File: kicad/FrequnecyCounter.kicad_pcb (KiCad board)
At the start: 4 copper layers, 130 x 90 mm, 138 parts, among them J1 USB_B, J2 CONN_COAXIAL, J3 CONN_COAXIAL, J4 CONN_COAXIAL, SW1 SW_Push, T1 WBC16-1T, U1 TPS650250, U10 MC12093, U11 tx176, U12 TLV3501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

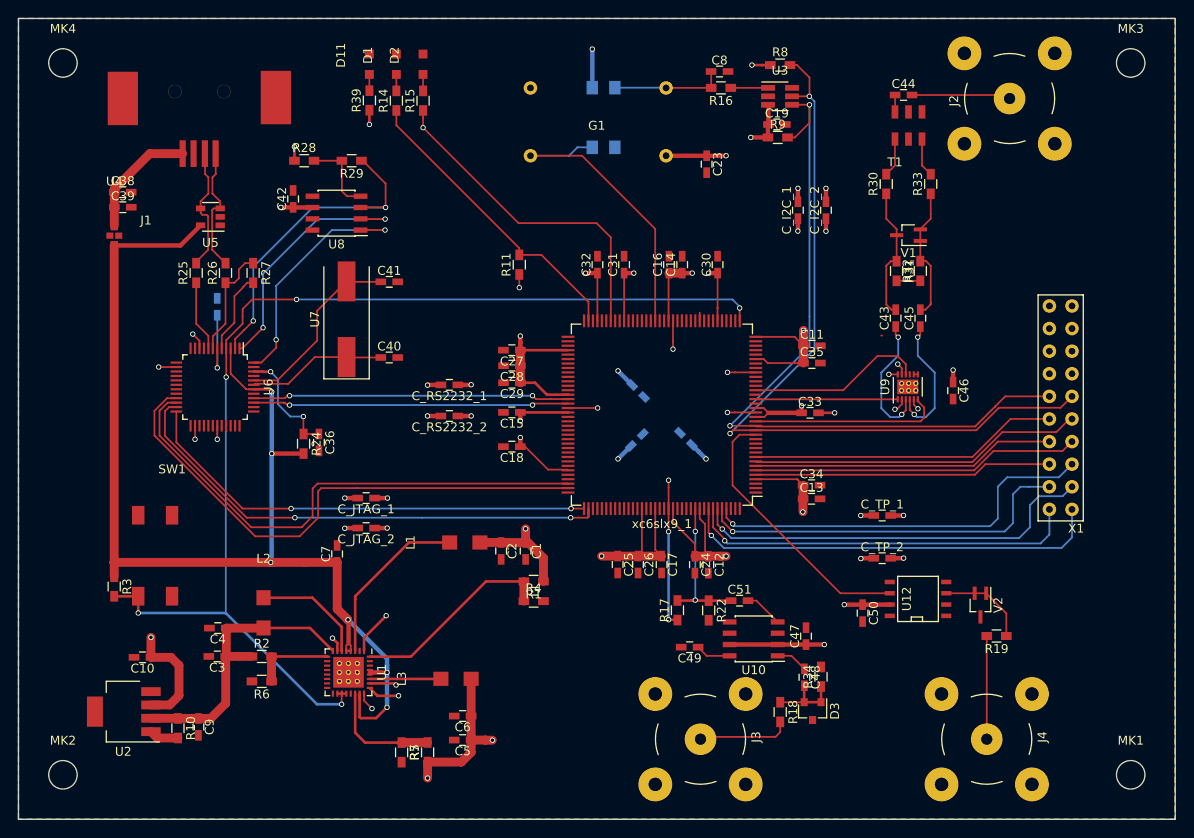
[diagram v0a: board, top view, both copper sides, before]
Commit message: Changed some Footprints to improve handsoldering
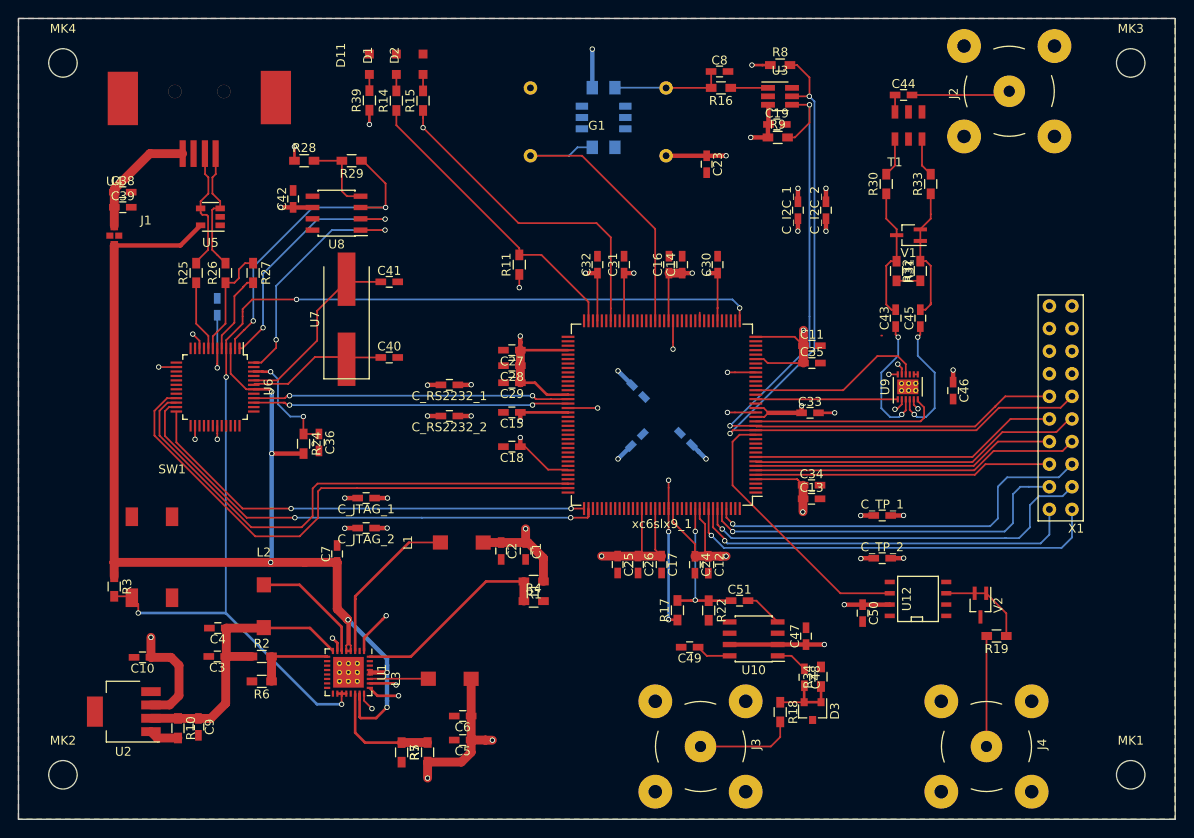
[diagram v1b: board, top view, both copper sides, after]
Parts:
- L2: footprint Footprints_LJ:LPS5030 -> LPS5030
- SW1: footprint Footprints_LJ:Mini-Taster-4pin -> Mini-Taster-4pin
- U11: footprint Footprints_LJ:tx176 -> tx176
- U7: footprint Crystals:Crystal_SMD_HC49-SD -> Crystal_SMD_HC49-SD
- moved J2 0.82 mm to (181.3, 64.2)
- moved J4 0.82 mm to (178.8, 137.8)
- moved J3 0.82 mm to (146.7, 137.8)
- moved L2 0.70 mm to (97.6, 120.4)
- moved L3 0.66 mm to (116.8, 130.2)
- moved L1 0.29 mm to (118.2, 114.9)
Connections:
- SW1 pad 2: GND -> (no net)
- SW1 pad 4: (no net) -> GND
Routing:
- net Net-(L3-Pad1): track 7.98 -> 6.58 mm
- net Net-(L1-Pad1): track 19.3 -> 18.2 mm
- net Net-(J4-Pad1): track 11.6 -> 12.4 mm
- net Net-(J3-Pad1): track 10.3 -> 11.1 mm
- net Net-(L2-Pad1): track 12.8 -> 13.4 mm
- net /FPGA/~RESET: track 127.1 -> 126.6 mm

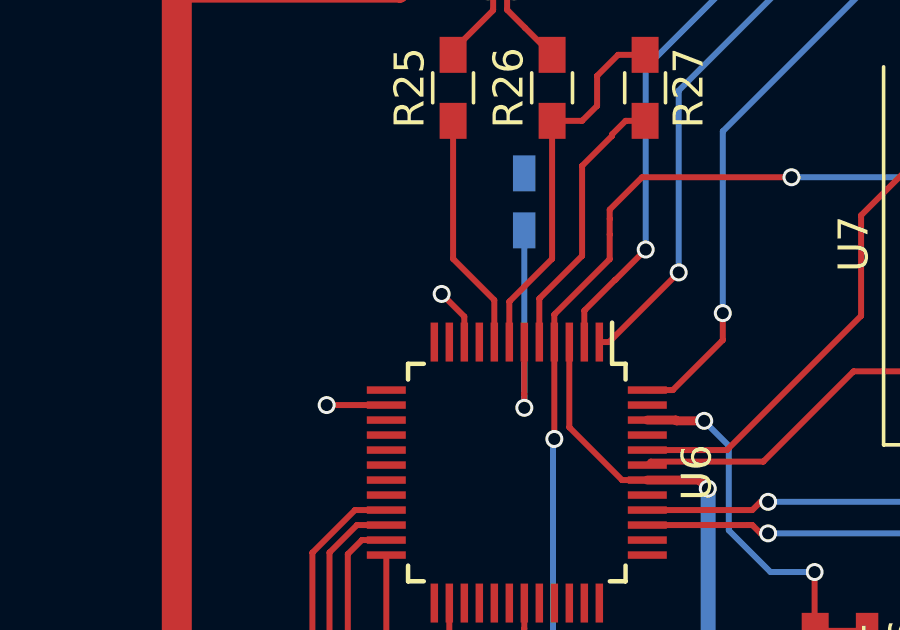
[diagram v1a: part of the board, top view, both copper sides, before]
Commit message: Small layout and schematic changes
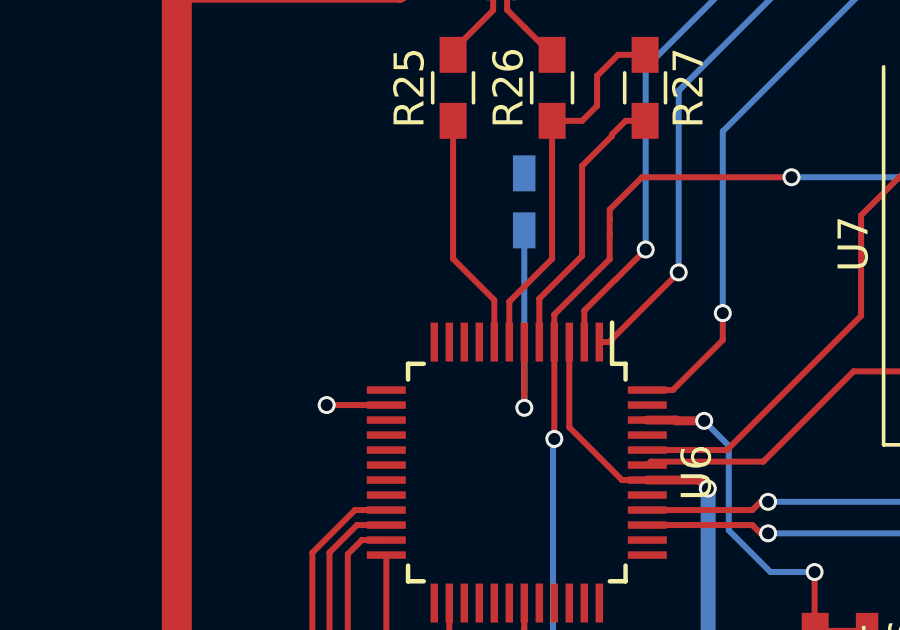
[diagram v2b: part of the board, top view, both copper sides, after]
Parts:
- R18, R19: value 100R -> 330R
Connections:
- U6 pad 10: +3V3 -> Net-(U6-Pad10)
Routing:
- net +3V3: track 77.3 -> 75.3 mm, vias 25 -> 24
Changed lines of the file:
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@@
 (kicad_pcb (version 4) (host pcbnew 4.0.6)
   (general
-    (links 366)
+    (links 365)
     (no_connects 0)
-    (area 39.150001 34.03 200.904763 155.795001)
+    (area 69.924999 55.924999 200.075001 146.075001)
     (thickness 1.6)
     (drawings 11)
-    (tracks 869)
+    (tracks 866)
     (zones 0)
     (modules 138)
-    (nets 191)
+    (nets 192)
   )
   (page A4)
@@
   (net 189 "Net-(xc6slx9_1-Pad39)")
   (net 190 "Net-(xc6slx9_1-Pad70)")
+  (net 191 "Net-(U6-Pad10)")
   (net_class Default "Dies ist die voreingestellte Netzklasse."
     (clearance 0.16)
@@
     (add_net "Net-(U5-Pad1)")
     (add_net "Net-(U6-Pad1)")
+    (add_net "Net-(U6-Pad10)")
     (add_net "Net-(U6-Pad11)")
     (add_net "Net-(U6-Pad12)")
@@
       (net 2 GND))
     (pad 10 smd rect (at -4.35 1.75 270) (size 1.3 0.25) (layers F.Cu F.Paste F.Mask)
-      (net 4 +3V3))
+      (net 191 "Net-(U6-Pad10)"))
     (pad 11 smd rect (at -4.35 2.25 270) (size 1.3 0.25) (layers F.Cu F.Paste F.Mask)
       (net 34 "Net-(U6-Pad11)"))
@@
       (effects (font (size 1 1) (thickness 0.15)))
     )
-    (fp_text value 100R (at 0 1.55 270) (layer F.Fab)
+    (fp_text value 330R (at 0 1.55 270) (layer F.Fab)
       (effects (font (size 1 1) (thickness 0.15)))
     )
@@
       (effects (font (size 1 1) (thickness 0.15)))
     )
-    (fp_text value 100R (at 0 1.55 180) (layer F.Fab)
+    (fp_text value 330R (at 0 1.55 180) (layer F.Fab)
       (effects (font (size 1 1) (thickness 0.15)))
     )
@@
   (via (at 89.8439 103.2961) (size 0.6) (drill 0.4) (layers F.Cu B.Cu) (net 4))
   (segment (start 89.8439 101.7742) (end 89.8439 103.2961) (width 0.2) (layer F.Cu) (net 4))
-  (via (at 89.5897 91.47) (size 0.6) (drill 0.4) (layers F.Cu B.Cu) (net 4))
-  (segment (start 90.3439 93.0742) (end 90.3439 92.2242) (width 0.2) (layer F.Cu) (net 4))
-  (segment (start 90.3439 92.2242) (end 89.5897 91.47) (width 0.2) (layer F.Cu) (net 4))
   (via (at 109.44 67.91) (size 0.6) (drill 0.4) (layers F.Cu B.Cu) (net 4))
   (segment (start 109.44 66.31) (end 109.44 67.91) (width 0.3) (layer F.Cu) (net 4))

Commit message: Small schematic and layout changes
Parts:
- removed SW1: SW_Push, Mini-Taster-4pin
- added C52: 100n, Capacitors_SMD:C_0603_HandSoldering, F.Cu at (172.0, 128.3)
- added Q1: BC846B, TO_SOT_Packages_SMD:SOT-23, F.Cu at (82.6, 120.7)
- added R12: 1k, Resistors_SMD:R_0603_HandSoldering, F.Cu at (78.3, 121.7)
- added R13: 150k, Resistors_SMD:R_0603_HandSoldering, F.Cu at (83.5, 116.6)
- added R20: R, Resistors_SMD:R_0603_HandSoldering, F.Cu at (178.1, 121.2)
- added R21: 100k, Resistors_SMD:R_0603_HandSoldering, F.Cu at (168.4, 128.5)
- added R23: 10k, Resistors_SMD:R_0603_HandSoldering, F.Cu at (170.2, 128.5)
- R18, R19: value 330R -> 3.3k
- R3: value 10k -> R
- moved R3 100.2 mm to (181.0, 121.2), turned to 90 degrees
- moved V2 3.13 mm to (179.7, 124.6), turned to 180 degrees
- moved C50 1.90 mm to (164.9, 124.7)
- moved U12 1.90 mm to (171.1, 123.1)
- moved R19 1.90 mm to (179.9, 127.3)
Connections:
- R3 pad 1: +5V -> /Signal_Input/CH_B
- R3 pad 2: /FPGA/~RESET -> +3V3
- U1 pad 18: /FPGA/~RESET -> /Power_Supply/~RESET
- U1 pad 19: /FPGA/~RESET -> /Power_Supply/~RESET
- U1 pad 20: /FPGA/~RESET -> /Power_Supply/~RESET
- U10 pad 3: GND -> /FPGA/DIV_SW2
- U10 pad 6: GND -> /FPGA/DIV_SW1
- U12 pad 2: GND -> Net-(C52-Pad1)
- U6 pad 10: Net-(U6-Pad10) -> +3V3
- U6 pad 4: /FPGA/~RESET -> +5V
- U8 pad 5: (no net) -> GND
- U8 pad 8: (no net) -> +3V3
- xc6slx9_1 pad 132: Net-(xc6slx9_1-Pad132) -> /FPGA/DIV_SW1
- xc6slx9_1 pad 143: Net-(xc6slx9_1-Pad143) -> /FPGA/DIV_SW2
- xc6slx9_1 pad 37: /FPGA/~RESET -> +3V3_FPGA
- xc6slx9_1 pad 65: Net-(xc6slx9_1-Pad65) -> +3V3_FPGA
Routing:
- net /FPGA/~RESET: track 126.6 -> 0.00 mm, vias 5 -> 0
- net /Power_Supply/~RESET: track 0.00 -> 44.0 mm, vias 0 -> 2
- net Net-(R13-Pad2): track 0.00 -> 25.6 mm, vias 0 -> 2
- net /FPGA/DIV_SW1: track 0.00 -> 18.3 mm, vias 0 -> 2
- net /FPGA/DIV_SW2: track 0.00 -> 18.1 mm
- net /FPGA/Clk_B: track 30.5 -> 42.5 mm
- net +3V3: track 75.3 -> 86.9 mm, vias 24 -> 28
- net Net-(C52-Pad1): track 0.00 -> 9.04 mm
- net +5V: track 137.9 -> 132.2 mm
- net +3V3_FPGA: track 155.3 -> 159.6 mm, vias 22 -> 23
- net Net-(Q1-Pad1): track 0.00 -> 2.00 mm
- net Net-(J4-Pad1): track 12.4 -> 10.5 mm
- net /Signal_Input/CH_B: track 10.2 -> 11.8 mm

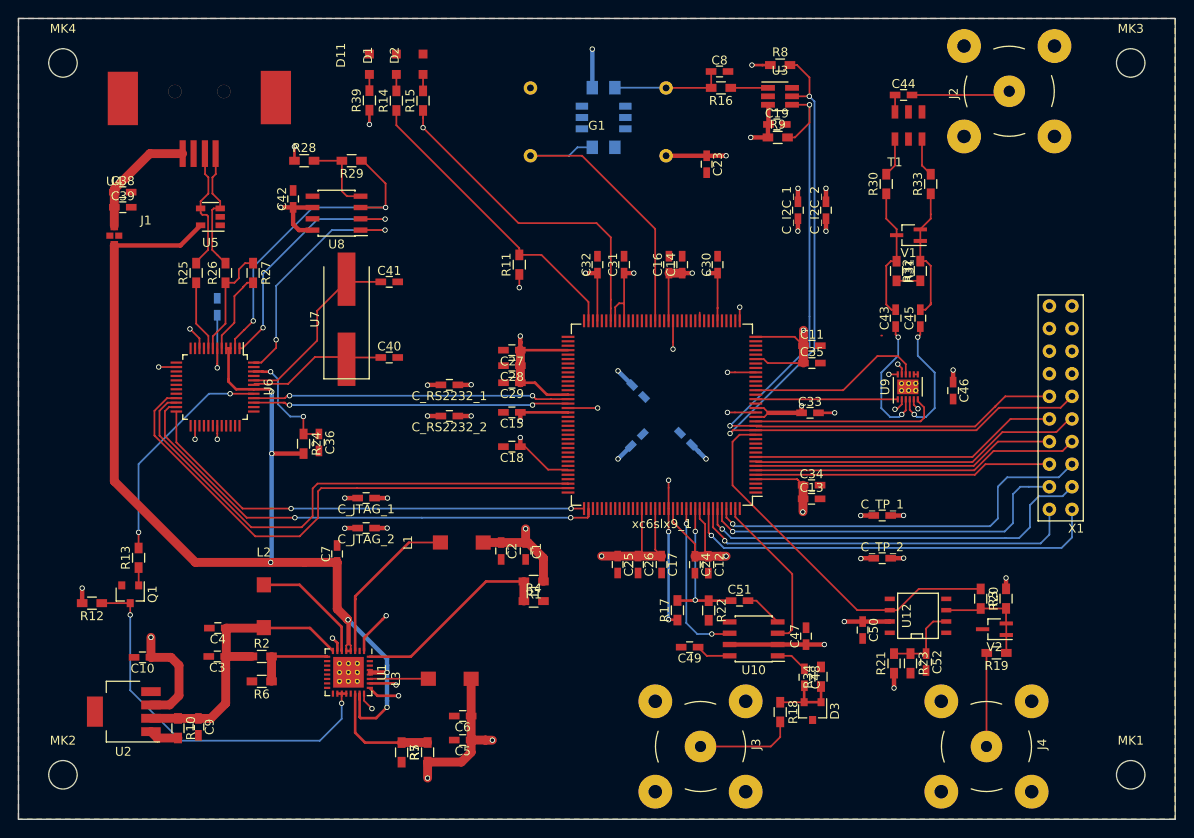
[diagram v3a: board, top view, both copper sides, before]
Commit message: Layout changes to guarantee the fit of the PCB housing
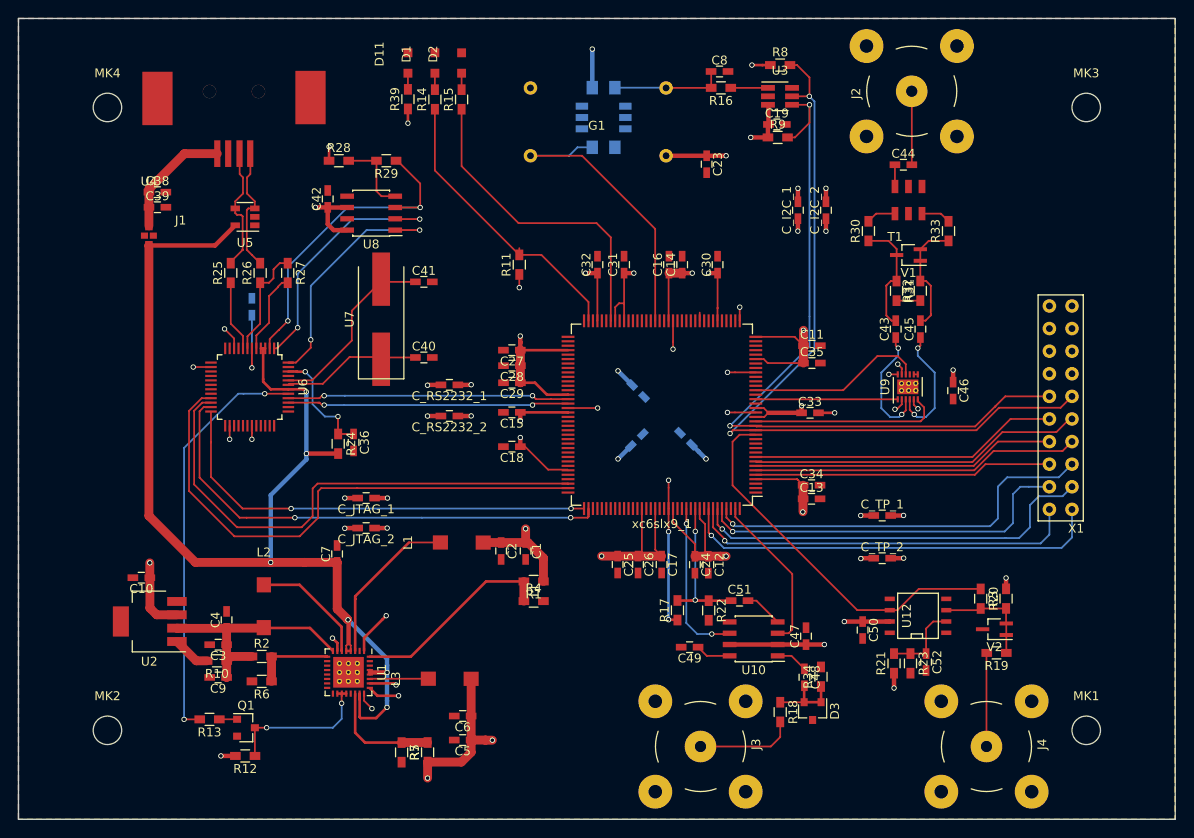
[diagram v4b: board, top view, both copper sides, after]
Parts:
- moved R12 24.3 mm to (95.5, 138.9)
- moved Q1 19.9 mm to (95.6, 135.7), turned to 0 degrees
- moved R13 19.8 mm to (91.5, 134.8), turned to 180 degrees
- moved J2 11.0 mm to (170.4, 64.2)
- moved U2 10.5 mm to (84.8, 123.8)
- moved C10 8.95 mm to (83.8, 118.8)
- moved R10 8.75 mm to (92.3, 128.2), turned to 180 degrees
- moved T1 8.38 mm to (168.5, 77.9)
- moved C44 7.84 mm to (169.4, 72.4)
- moved MK1 7.07 mm to (190.0, 136.0)
- moved MK2 7.07 mm to (80.0, 136.0)
- moved MK3 7.07 mm to (190.0, 66.0)
- moved MK4 7.07 mm to (80.0, 66.0)
- moved C9 5.98 mm to (92.4, 130.1), turned to 180 degrees
- moved R30 5.66 mm to (165.5, 79.9)
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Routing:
- net /Power_Supply/~RESET: track 44.0 -> 17.2 mm
- net Net-(R13-Pad2): track 25.6 -> 46.5 mm
- net +3V6: track 33.4 -> 27.3 mm
- net (no net): track 752.2 -> 747.2 mm
- net +3V3: track 86.9 -> 82.5 mm
- net /USB_JTAG/RXD: track 35.5 -> 31.6 mm
- net /FPGA/RXD: track 35.6 -> 31.7 mm
- net /Signal_Input/Ext_Ref: track 11.1 -> 8.28 mm
- net /Signal_Input/V1-: track 15.3 -> 13.3 mm
- net /Signal_Input/V1+: track 15.1 -> 13.2 mm
- net WORK_LED: track 37.5 -> 35.9 mm, vias 1 -> 0
- net /FPGA/TCK: track 52.4 -> 50.8 mm
- net /Signal_Input/IN-: track 14.8 -> 13.6 mm
- net /Signal_Input/IN+: track 14.8 -> 13.6 mm
- net /FPGA/TDI: track 57.5 -> 56.4 mm
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
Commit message: Changed layout to guarantee to fit the housing
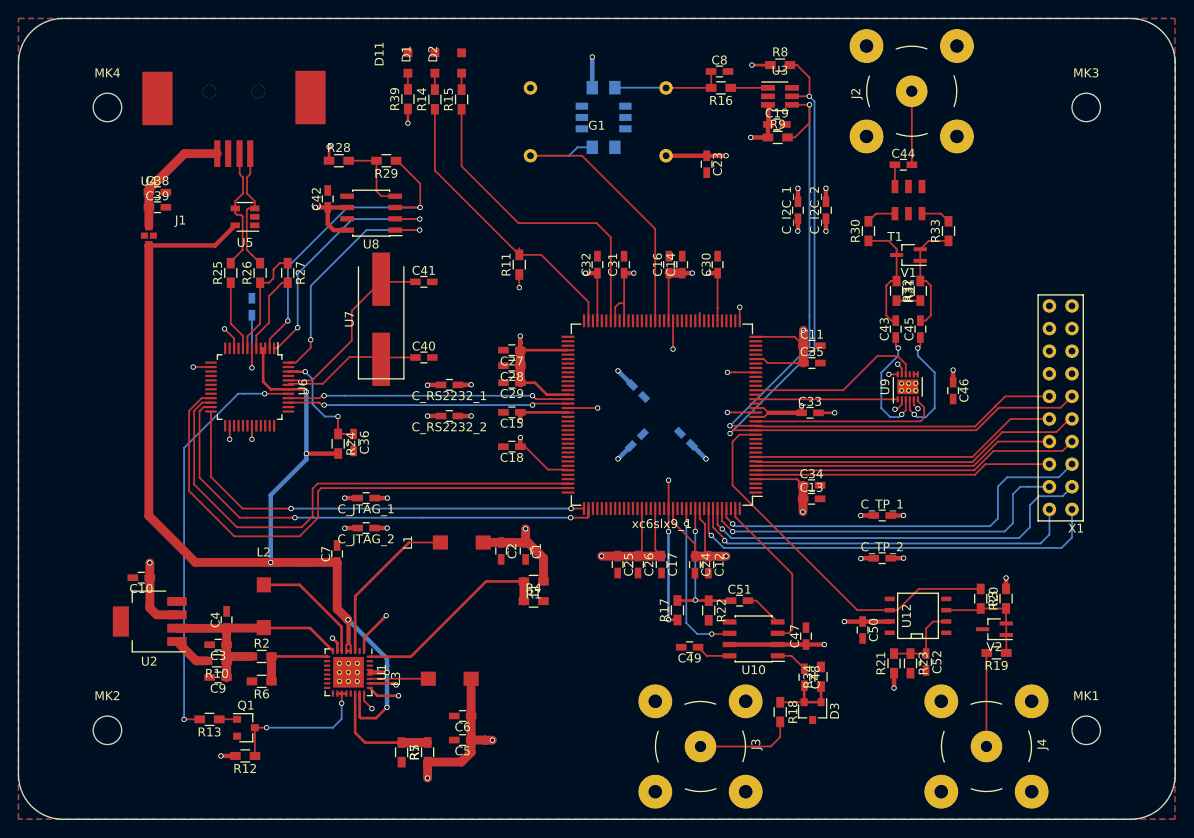
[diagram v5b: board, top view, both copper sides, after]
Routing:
- net (no net): track 747.2 -> 778.9 mm
- net +3V3: track 82.5 -> 81.6 mm
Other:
- outline, holes or cut-outs redrawn
